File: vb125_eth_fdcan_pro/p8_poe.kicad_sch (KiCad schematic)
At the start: 16 parts, among them Q5 2N7002, T1 PA1134NL, U10 PS2911-1-F3-AX, U12 ZR431, U9 LTC4267

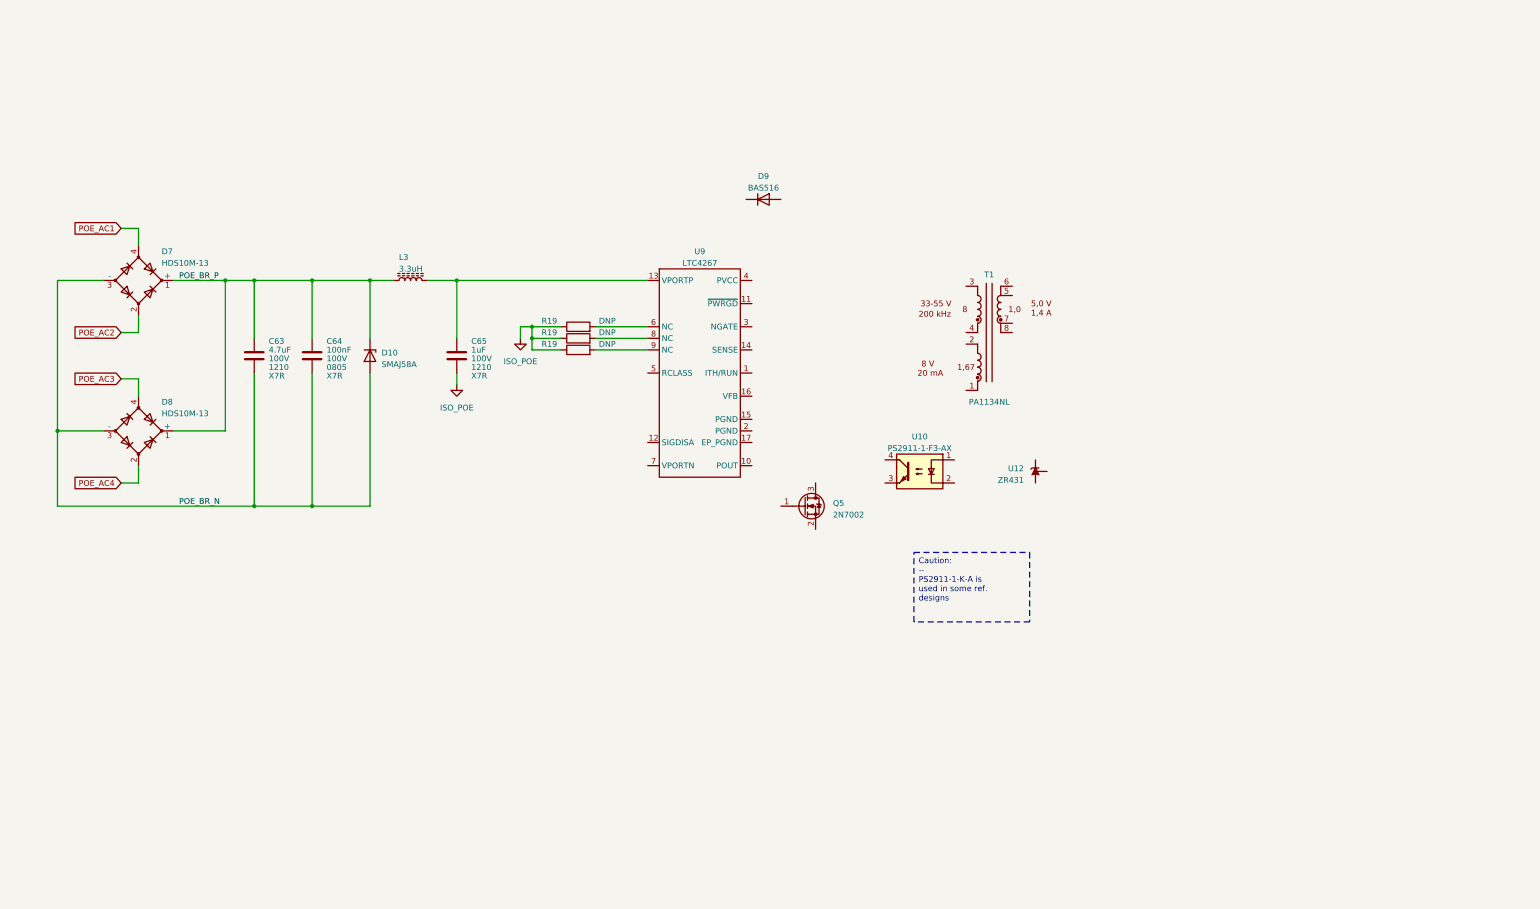
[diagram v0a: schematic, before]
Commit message: Finish PoE schematic.
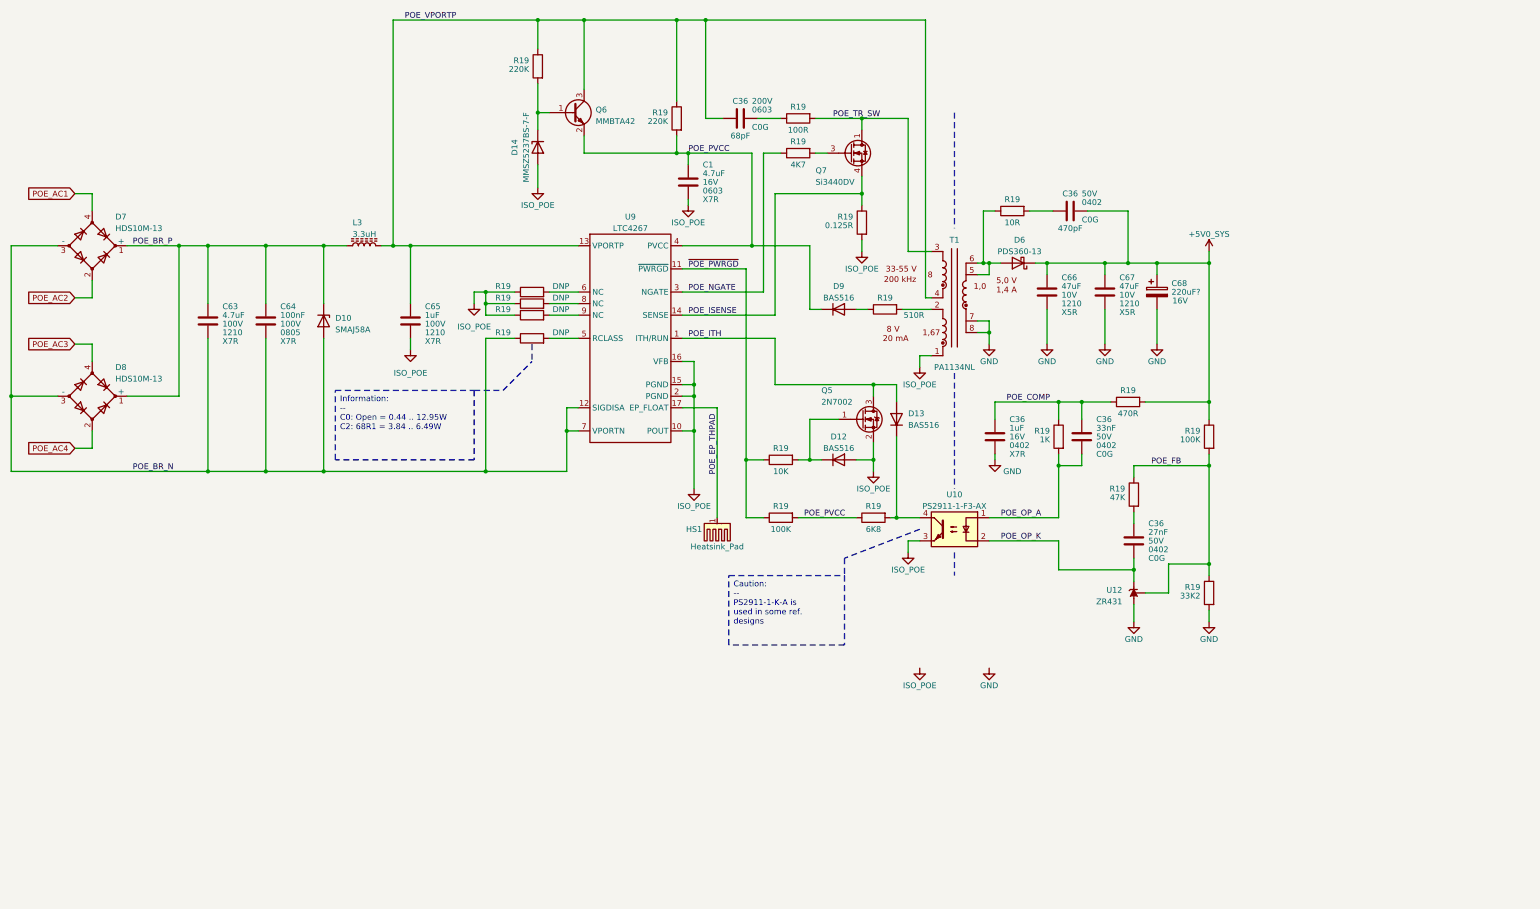
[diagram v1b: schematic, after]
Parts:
- added C1: 4.7uF, Capacitor_SMD:C_0603_1608Metric, symbol Device:C
- added C36: 68pF, Capacitor_SMD:C_0603_1608Metric, symbol Device:C
- added C36: 470pF, symbol Device:C
- added C36: 1uF, symbol Device:C
- added C36: 27nF, symbol Device:C
- added C36: 33nF, symbol Device:C
- added C66, C67: 47uF, Capacitor_SMD:C_1210_3225Metric, symbol Device:C
- added C68: 220uF?, Capacitor_SMD:CP_Elec_6.3x7.7, symbol Device:C_Polarized
- added D12, D13: BAS516, Diode_SMD:D_SOD-523, symbol Diode:BAS516
- added D14: MMSZ5237BS-7-F, Diode_SMD:D_SOD-323, symbol Device:D_Zener
- added D6: PDS360-13, Diode_SMD:D_PowerDI-5, symbol Device:D_Schottky
- added HS1: Heatsink_Pad, symbol Mechanical:Heatsink_Pad
- added Q6: MMBTA42, Package_TO_SOT_SMD:SOT-23, symbol Transistor_BJT:MMBTA42
- added Q7: Si3440DV, Package_SO:TSOP-6_1.65x3.05mm_P0.95mm, symbol Transistor_FET:Si3456DDV
- added R19 (x2): 220K, Resistor_SMD:R_0402_1005Metric, symbol Device:R
- added R19: 100R, Resistor_SMD:R_0805_2012Metric, symbol Device:R
- added R19: 10R, Resistor_SMD:R_0603_1608Metric, symbol Device:R
- added R19: 33K2, Resistor_SMD:R_0402_1005Metric, symbol Device:R
- added R19: 1K, Resistor_SMD:R_0402_1005Metric, symbol Device:R
- added R19: 0.125R, Resistor_SMD:R_1206_3216Metric, symbol Device:R
- added R19 (x2): 100K, Resistor_SMD:R_0402_1005Metric, symbol Device:R
- added R19: 470R, Resistor_SMD:R_0402_1005Metric, symbol Device:R
- added R19: 510R, Resistor_SMD:R_0402_1005Metric, symbol Device:R
- added R19: DNP, Resistor_SMD:R_0402_1005Metric, symbol Device:R
- added R19: 10K, Resistor_SMD:R_0402_1005Metric, symbol Device:R
- added R19: 4K7, Resistor_SMD:R_0402_1005Metric, symbol Device:R
- added R19: 6K8, Resistor_SMD:R_0402_1005Metric, symbol Device:R
- added R19: 47K, Resistor_SMD:R_0402_1005Metric, symbol Device:R
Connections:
- net ISO_POE: now also Q5.2 (S), T1.1, U10.3, U9.10 (POUT), U9.15 (PGND), U9.16 (VFB), U9.2 (PGND), C1.2, D12.2 (A), D14.2 (A), R19.2
- net POE_BR_N: now also U9.12 (SIGDISA), U9.7 (VPORTN), R19.1
- net at T1.2: now also R19.2
- net POE_TR_SW: now reaches T1.3
- net POE_TR_SW: now also Q7.1 (D), Q7.2 (D), Q7.5 (D), Q7.6 (D), R19.2
- net POE_VPORTP: now reaches T1.4
- net POE_VPORTP: now also C65.1, L3.2, U9.13 (VPORTP), C36.1, Q6.3 (C), R19.1, R19.1
- net at T1.5: now also T1.6, D6.2 (A), R19.1
- net GND: now reaches T1.7
- net GND: now also T1.8, U12.3 (A), C36.2, C66.2, C67.2, C68.2, R19.2
- net POE_PVCC: now reaches D9.1 (K)
- net POE_PVCC: now also U9.4 (PVCC), C1.1, Q6.2 (E), R19.1, R19.2, R19.2
- net at D9.2 (A): now also R19.1
- net POE_FB: now reaches U12.1 (REF)
- net POE_FB: now also R19.1, R19.1, R19.2
- net POE_OP_K: now reaches U12.2 (K)
- net POE_OP_K: now also U10.2, C36.2
- net POE_OP_A: now reaches U10.1
- net POE_OP_A: now also C36.2, R19.2
- net at U10.4: now also D13.1 (K), R19.2
- net at Q5.1 (G): now also D12.1 (K), R19.2
- net POE_ITH: now reaches Q5.3 (D)
- net POE_ITH: now also U9.1 (ITH/RUN), D13.2 (A)
- net ~{POE_PWRGD}: now reaches U9.11 (~{PWRGD})
- net ~{POE_PWRGD}: now also R19.1, R19.1
- net POE_ISENSE: now reaches U9.14 (SENSE)
- net POE_ISENSE: now also Q7.4 (S), R19.1
- net POE_EP_THPAD: now reaches U9.17 (EP_FLOAT)
- net POE_EP_THPAD: now also HS1.1
- net POE_NGATE: now reaches U9.3 (NGATE)
- net POE_NGATE: now also R19.1
- net at U9.5 (RCLASS): now also R19.2
- new net: C36.2, R19.1
- new net: D14.1 (K), Q6.1 (B), R19.2
- new net: C36.1, R19.2 (x2)
- new net: Q7.3 (G), R19.2
- new net +5V0_SYS: C36.2, C66.1, C67.1, C68.1, D6.1 (K), R19.1, R19.2
- new net POE_COMP: C36.1, C36.1, R19.1, R19.1
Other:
- moved on the sheet: C63, C64, C65, D10, D7, D8, D9, L3, Q5, R19, T1, U10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

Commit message: Finish schematics.
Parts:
- added C101: Y rated, THT, Capacitor_THT:C_Disc_D7.0mm_W2.5mm_P5.00mm, symbol Device:C
- added C103: Y rated, SMD 1808, vhrd_generic:C_1808_4520Metric, symbol Device:C
- C36: footprint (none) -> Capacitor_SMD:C_0402_1005Metric
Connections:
- net GND: now also C101.2, C103.2
- net ISO_POE: now also C101.1, C103.1
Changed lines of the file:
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@@
   (junction (at 129.54 16.51) (diameter 0) (color 0 0 0 0)
   )
+  (junction (at 207.01 151.13) (diameter 0) (color 0 0 0 0)
+  )
   (junction (at 227.33 69.85) (diameter 0) (color 0 0 0 0)
   )
@@
   (junction (at 82.55 115.57) (diameter 0) (color 0 0 0 0)
   )
+  (junction (at 234.95 151.13) (diameter 0) (color 0 0 0 0)
+  )
   (junction (at 160.02 16.51) (diameter 0) (color 0 0 0 0)
   )
@@
   )
   (wire (pts (xy 139.7 45.72) (xy 160.02 45.72))
+    (stroke (width 0) (type default))
+  )
+  (wire (pts (xy 224.79 146.05) (xy 234.95 146.05))
     (stroke (width 0) (type default))
   )
@@
     (stroke (width 0) (type default))
   )
+  (wire (pts (xy 234.95 160.02) (xy 234.95 151.13))
+    (stroke (width 0) (type default))
+  )
   (wire (pts (xy 213.36 90.17) (xy 215.9 90.17))
     (stroke (width 0) (type default))
@@
     (stroke (width 0) (type default))
   )
+  (wire (pts (xy 207.01 160.02) (xy 207.01 151.13))
+    (stroke (width 0) (type default))
+  )
   (wire (pts (xy 226.06 72.39) (xy 228.6 72.39))
     (stroke (width 0) (type default))
@@
   )
   (wire (pts (xy 226.06 82.55) (xy 228.6 82.55))
+    (stroke (width 0) (type default))
+  )
+  (wire (pts (xy 234.95 151.13) (xy 234.95 146.05))
     (stroke (width 0) (type default))
   )
@@
     (stroke (width 0) (type default))
   )
+  (wire (pts (xy 207.01 151.13) (xy 207.01 146.05))
+    (stroke (width 0) (type default))
+  )
   (wire (pts (xy 97.79 16.51) (xy 97.79 66.04))
     (stroke (width 0) (type default))
@@
     (stroke (width 0) (type default))
   )
+  (wire (pts (xy 224.79 151.13) (xy 234.95 151.13))
+    (stroke (width 0) (type default))
+  )
   (wire (pts (xy 69.85 115.57) (xy 57.15 115.57))
     (stroke (width 0) (type default))
@@
   )
   (wire (pts (xy 118.11 86.36) (xy 118.11 115.57))
+    (stroke (width 0) (type default))
+  )
+  (wire (pts (xy 207.01 151.13) (xy 217.17 151.13))
     (stroke (width 0) (type default))
   )
@@
   )
   (wire (pts (xy 27.94 87.63) (xy 31.75 87.63))
+    (stroke (width 0) (type default))
+  )
+  (wire (pts (xy 207.01 146.05) (xy 217.17 146.05))
     (stroke (width 0) (type default))
   )
@@
     )
   )
-  (symbol (lib_id "vhrd_power:ISO_POE") (at 213.36 158.75 0) (unit 1)
-    (in_bom yes) (on_board yes) (dnp no)
-    (property "Reference" "#PWR0135" (at 213.36 165.1 0)
-      (effects (font (size 1.27 1.27)) hide)
-    )
-    (property "Value" "ISO_POE" (at 213.36 162.56 0)
-      (effects (font (size 1.27 1.27)))
-    )
-    (property "Footprint" "" (at 213.36 158.75 0)
-      (effects (font (size 1.27 1.27)) hide)
-    )
-    (property "Datasheet" "" (at 213.36 158.75 0)
+  (symbol (lib_id "vhrd_power:ISO_POE") (at 207.01 160.02 0) (unit 1)
+    (in_bom yes) (on_board yes) (dnp no)
+    (property "Reference" "#PWR0135" (at 207.01 166.37 0)
+      (effects (font (size 1.27 1.27)) hide)
+    )
+    (property "Value" "ISO_POE" (at 207.01 163.83 0)
+      (effects (font (size 1.27 1.27)))
+    )
+    (property "Footprint" "" (at 207.01 160.02 0)
+      (effects (font (size 1.27 1.27)) hide)
+    )
+    (property "Datasheet" "" (at 207.01 160.02 0)
       (effects (font (size 1.27 1.27)) hide)
     )
@@
     )
   )
+  (symbol (lib_id "Device:C") (at 220.98 151.13 90) (mirror x) (unit 1)
+    (in_bom yes) (on_board yes) (dnp no)
+    (property "Reference" "C103" (at 219.71 154.94 90)
+      (effects (font (size 1.27 1.27)) (justify left))
+    )
+    (property "Value" "Y rated, SMD 1808" (at 214.63 157.48 90)
+      (effects (font (size 1.27 1.27)) (justify right))
+    )
+    (property "Footprint" "vhrd_generic:C_1808_4520Metric" (at 224.79 152.0952 0)
+      (effects (font (size 1.27 1.27)) hide)
+    )
+    (property "Datasheet" "~" (at 220.98 151.13 0)
+      (effects (font (size 1.27 1.27)) hide)
+    )
+    (pin "1")
+    (pin "2")
+    (instances
+      (project "vb125_eth_fdcan_pro"
+        (path "/b473bccb-f14c-41d5-b473-137d3ef8ae1e/96773d61-2940-42cb-9a0c-01cb58b4a4b5"
+          (reference "C103") (unit 1)
+        )
+        (path "/b473bccb-f14c-41d5-b473-137d3ef8ae1e/1ac386c6-64ba-4865-8e07-7f3718b45cdc"
+          (reference "C104") (unit 1)
+        )
+        (path "/b473bccb-f14c-41d5-b473-137d3ef8ae1e/5caca214-bd98-4d53-9e0b-a904082b09c6"
+          (reference "C114") (unit 1)
+        )
+      )
+    )
+  )
   (symbol (lib_id "Device:C") (at 162.56 52.07 0) (unit 1)
     (in_bom yes) (on_board yes) (dnp no)
@@
     )
   )
+  (symbol (lib_id "Device:C") (at 220.98 146.05 90) (unit 1)
+    (in_bom yes) (on_board yes) (dnp no) (fields_autoplaced)
+    (property "Reference" "C101" (at 215.0121 139.7 90)
+      (effects (font (size 1.27 1.27)) (justify right))
+    )
+    (property "Value" "Y rated, THT" (at 226.9479 142.24 90)
+      (effects (font (size 1.27 1.27)) (justify left))
+    )
+    (property "Footprint" "Capacitor_THT:C_Disc_D7.0mm_W2.5mm_P5.00mm" (at 224.79 145.0848 0)
+      (effects (font (size 1.27 1.27)) hide)
+    )
+    (property "Datasheet" "~" (at 220.98 146.05 0)
+      (effects (font (size 1.27 1.27)) hide)
+    )
+    (pin "1")
+    (pin "2")
+    (instances
+      (project "vb125_eth_fdcan_pro"
+        (path "/b473bccb-f14c-41d5-b473-137d3ef8ae1e/96773d61-2940-42cb-9a0c-01cb58b4a4b5"
+          (reference "C101") (unit 1)
+        )
+        (path "/b473bccb-f14c-41d5-b473-137d3ef8ae1e/1ac386c6-64ba-4865-8e07-7f3718b45cdc"
+          (reference "C102") (unit 1)
+        )
+        (path "/b473bccb-f14c-41d5-b473-137d3ef8ae1e/5caca214-bd98-4d53-9e0b-a904082b09c6"
+          (reference "C113") (unit 1)
+        )
+      )
+    )
+  )
   (symbol (lib_id "Device:R") (at 128.27 78.74 90) (unit 1)
     (in_bom yes) (on_board yes) (dnp no)
@@
       (effects (font (size 1.27 1.27)))
     )
-    (property "Footprint" "" (at 250.19 57.4548 0)
+    (property "Footprint" "Capacitor_SMD:C_0402_1005Metric" (at 250.19 57.4548 0)
       (effects (font (size 1.27 1.27)) hide)
     )
@@
     )
   )
-  (symbol (lib_id "power:GND") (at 228.6 158.75 0) (unit 1)
-    (in_bom yes) (on_board yes) (dnp no)
-    (property "Reference" "#PWR09" (at 228.6 165.1 0)
-      (effects (font (size 1.27 1.27)) hide)
-    )
-    (property "Value" "GND" (at 228.6 162.56 0)
-      (effects (font (size 1.27 1.27)))
-    )
-    (property "Footprint" "" (at 228.6 158.75 0)
-      (effects (font (size 1.27 1.27)) hide)
-    )
-    (property "Datasheet" "" (at 228.6 158.75 0)
+  (symbol (lib_id "power:GND") (at 234.95 160.02 0) (unit 1)
+    (in_bom yes) (on_board yes) (dnp no)
+    (property "Reference" "#PWR09" (at 234.95 166.37 0)
+      (effects (font (size 1.27 1.27)) hide)
+    )
+    (property "Value" "GND" (at 234.95 163.83 0)
+      (effects (font (size 1.27 1.27)))
+    )
+    (property "Footprint" "" (at 234.95 160.02 0)
+      (effects (font (size 1.27 1.27)) hide)
+    )
+    (property "Datasheet" "" (at 234.95 160.02 0)
       (effects (font (size 1.27 1.27)) hide)
     )
@@
       (effects (font (size 1.27 1.27)) (justify left))
     )
-    (property "Footprint" "" (at 230.8352 111.76 0)
+    (property "Footprint" "Capacitor_SMD:C_0402_1005Metric" (at 230.8352 111.76 0)
       (effects (font (size 1.27 1.27)) hide)
     )
@@
       (effects (font (size 1.27 1.27)) (justify left))
     )
-    (property "Footprint" "" (at 261.3152 134.62 0)
+    (property "Footprint" "Capacitor_SMD:C_0402_1005Metric" (at 261.3152 134.62 0)
       (effects (font (size 1.27 1.27)) hide)
     )
@@
       (effects (font (size 1.27 1.27)) (justify left))
     )
-    (property "Footprint" "" (at 249.8852 111.76 0)
-      (effects (font (size 1.27 1.27)) hide)
-    )
+    (property "Footprint" "Capacitor_SMD:C_0402_1005Metric" (at 249.8852 111.76 0)
+      (effects (font (size 1.27 1.27)) hide)
+    )
